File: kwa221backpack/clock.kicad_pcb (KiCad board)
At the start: 2 copper layers, 58.4 x 81.3 mm, 5 parts, among them P1 CONN_01X10, P2 CONN_01X10, U1 TLC5940NT

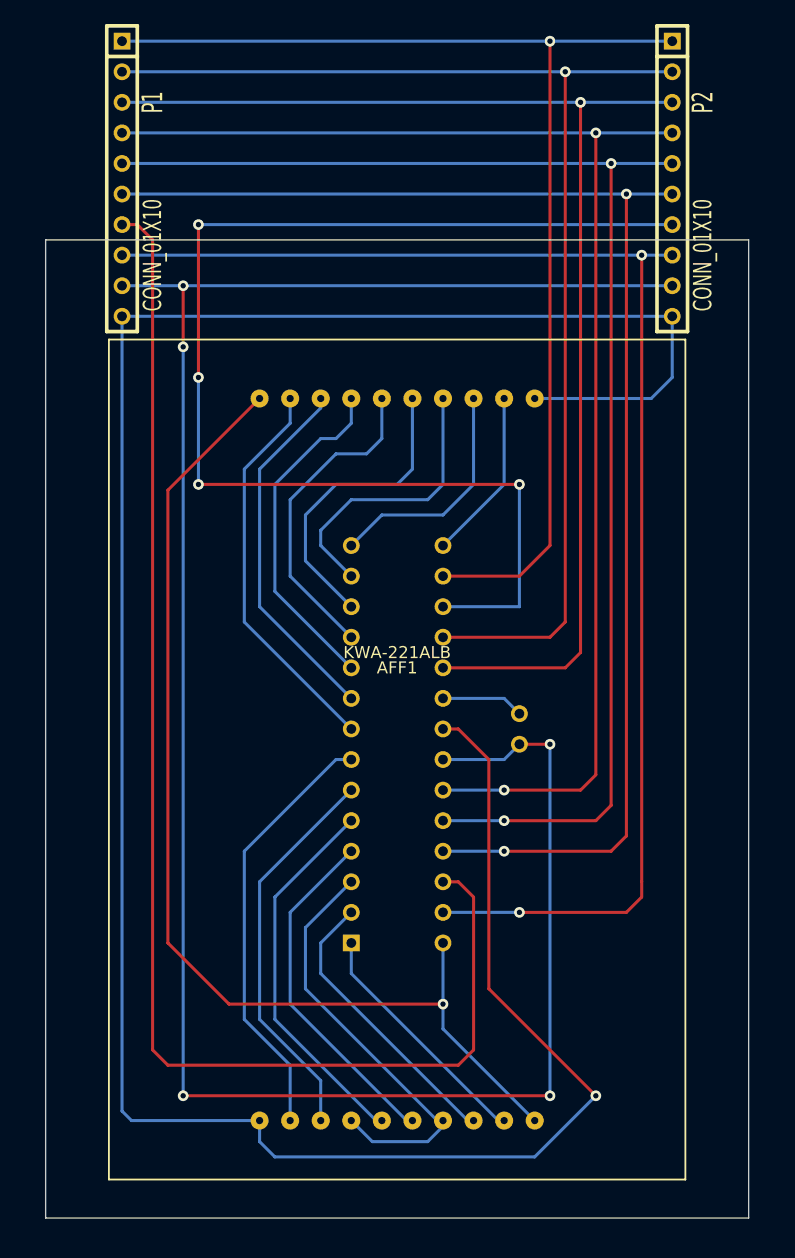
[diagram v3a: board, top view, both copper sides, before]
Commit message: Managed to route all the traces under the LED
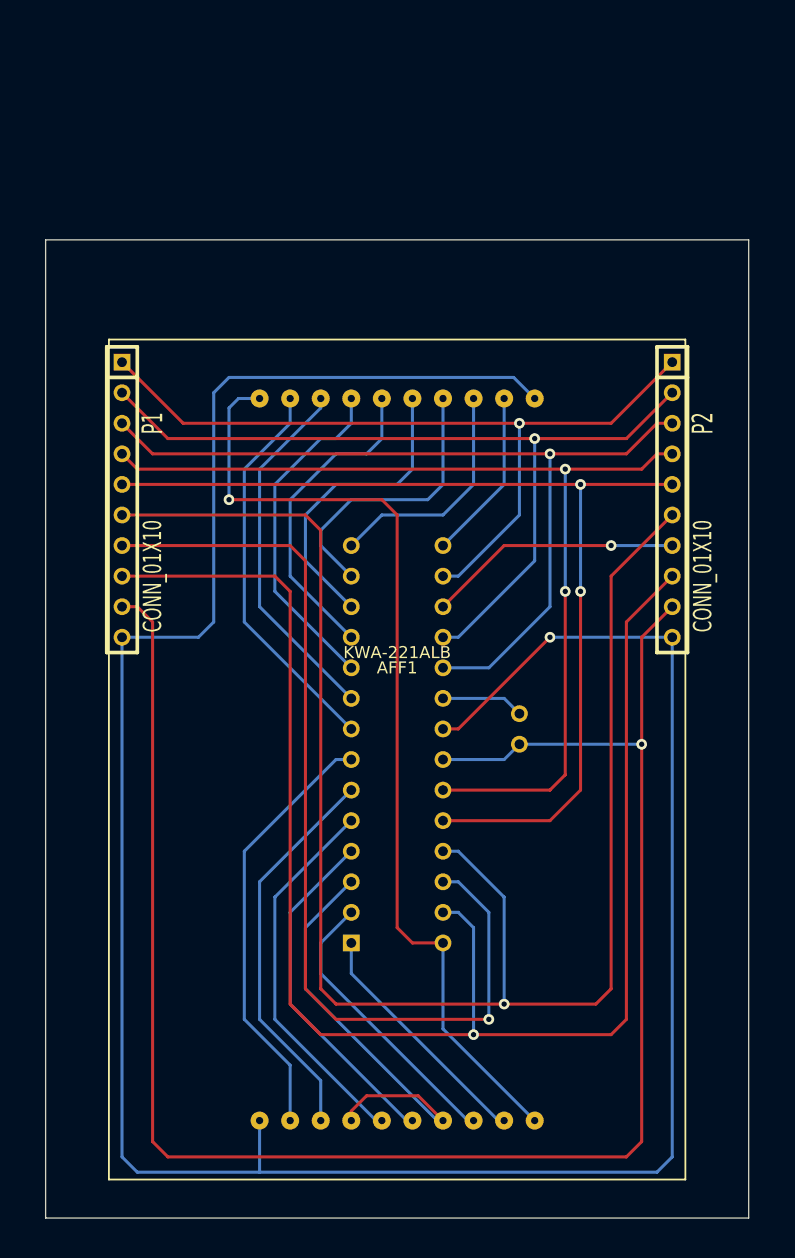
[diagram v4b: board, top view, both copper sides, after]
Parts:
- moved P1 26.7 mm to (49.5, 52.1)
- moved P2 26.7 mm to (95.2, 52.1)
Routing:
- net /SOUT: track 104.1 -> 21.2 mm, vias 4 -> 1
- net /GSCLK: track 102.1 -> 69.3 mm
- net /SIN: track 113.9 -> 81.4 mm, vias 0 -> 1
- net /DCPRG: track 103.4 -> 71.5 mm
- net GND: track 182.1 -> 150.5 mm, vias 5 -> 1
- net /XERR: track 97.6 -> 66.0 mm
- net /XLAT: track 113.6 -> 83.6 mm
- net /BLANK: track 112.3 -> 82.9 mm
- net /SCLK: track 114.8 -> 137.3 mm, vias 2 -> 1
- net /VPRG: track 116.1 -> 128.7 mm, vias 2 -> 1
- net /D0: track 91.3 -> 81.5 mm
- net VCC: track 209.6 -> 214.7 mm

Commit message: More tweaking, allow 3D to render better
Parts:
- P1, P2: moved to B.Cu
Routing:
- net GND: track 150.5 -> 132.7 mm
- net VCC: track 214.7 -> 197.3 mm
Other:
- board size 58.4 x 81.3 mm -> 48.3 x 71.1 mm

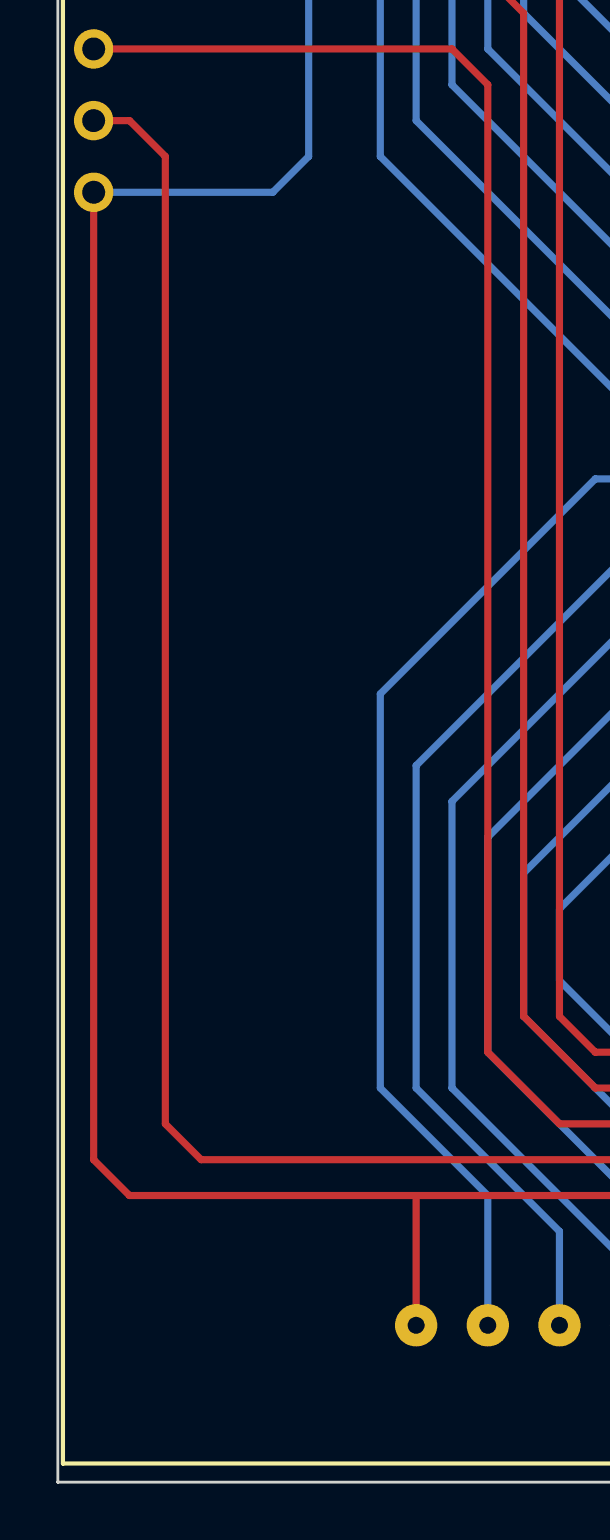
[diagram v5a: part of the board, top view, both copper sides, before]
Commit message: Export Gerber/VRML
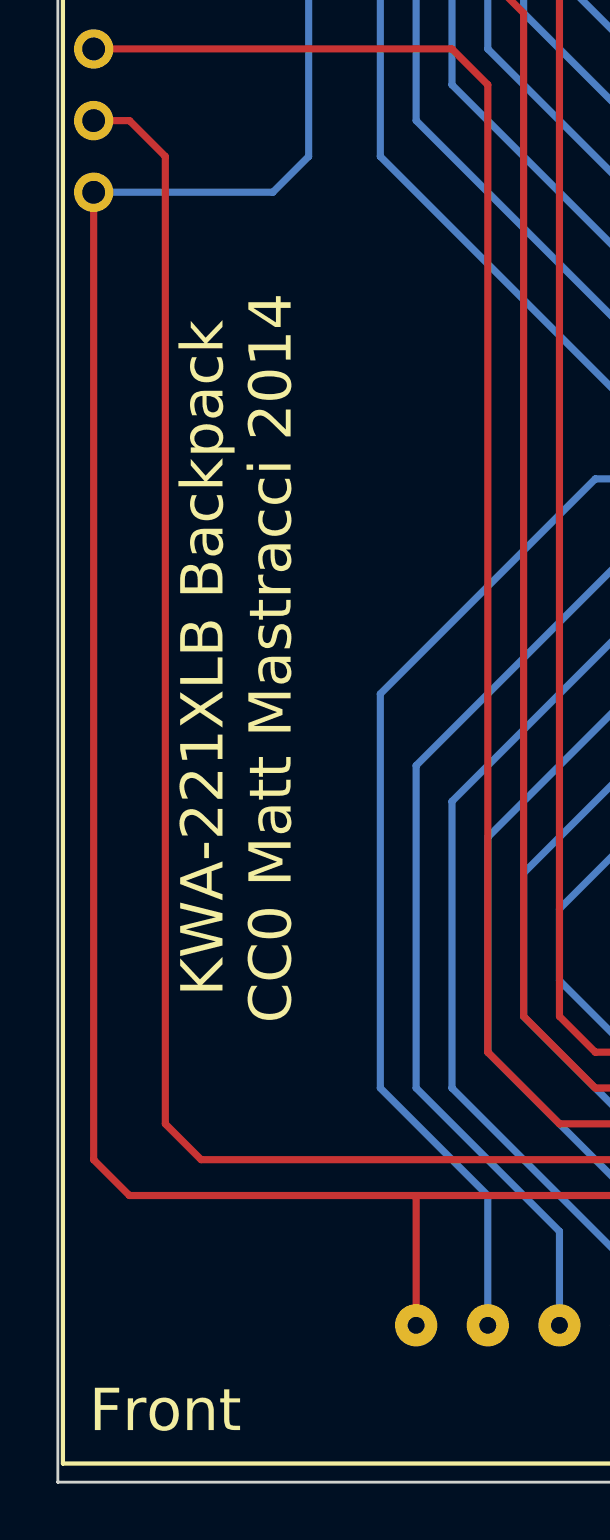
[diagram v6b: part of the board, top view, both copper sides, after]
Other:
- board text added: "Back"
- board text added: "Front"
- board text added: "KWA-221XLB Backpack CC0 Matt Mastracci 2014"
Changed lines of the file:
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@@
     (links 42)
     (no_connects 0)
-    (area 45.71873 38.049999 96.926401 109.270001)
+    (area 39.924287 38.049999 96.926401 109.270001)
     (thickness 1.6)
-    (drawings 4)
+    (drawings 8)
     (tracks 196)
     (zones 0)
@@
       (outputformat 1)
       (mirror false)
-      (drillshape 1)
+      (drillshape 0)
       (scaleselection 1)
-      (outputdirectory ""))
+      (outputdirectory gerber))
   )
   (net 0 "")
@@
     )
   )
+  (gr_text "KWA-221XLB Backpack\nCC0 Matt Mastracci 2014" (at 54.61 80.01 90) (layer B.SilkS)
+    (effects (font (size 1.5 1.5) (thickness 0.3)) (justify mirror))
+  )
+  (gr_text Back (at 92.71 106.68) (layer B.SilkS)
+    (effects (font (size 1.5 1.5) (thickness 0.3)) (justify mirror))
+  )
+  (gr_text Front (at 52.07 106.68) (layer F.SilkS)
+    (effects (font (size 1.5 1.5) (thickness 0.3)))
+  )
+  (gr_text "KWA-221XLB Backpack\nCC0 Matt Mastracci 2014" (at 54.61 80.01 90) (layer F.SilkS)
+    (effects (font (size 1.5 1.5) (thickness 0.3)))
+  )
   (gr_line (start 96.52 38.1) (end 48.26 38.1) (angle 90) (layer Edge.Cuts) (width 0.1))

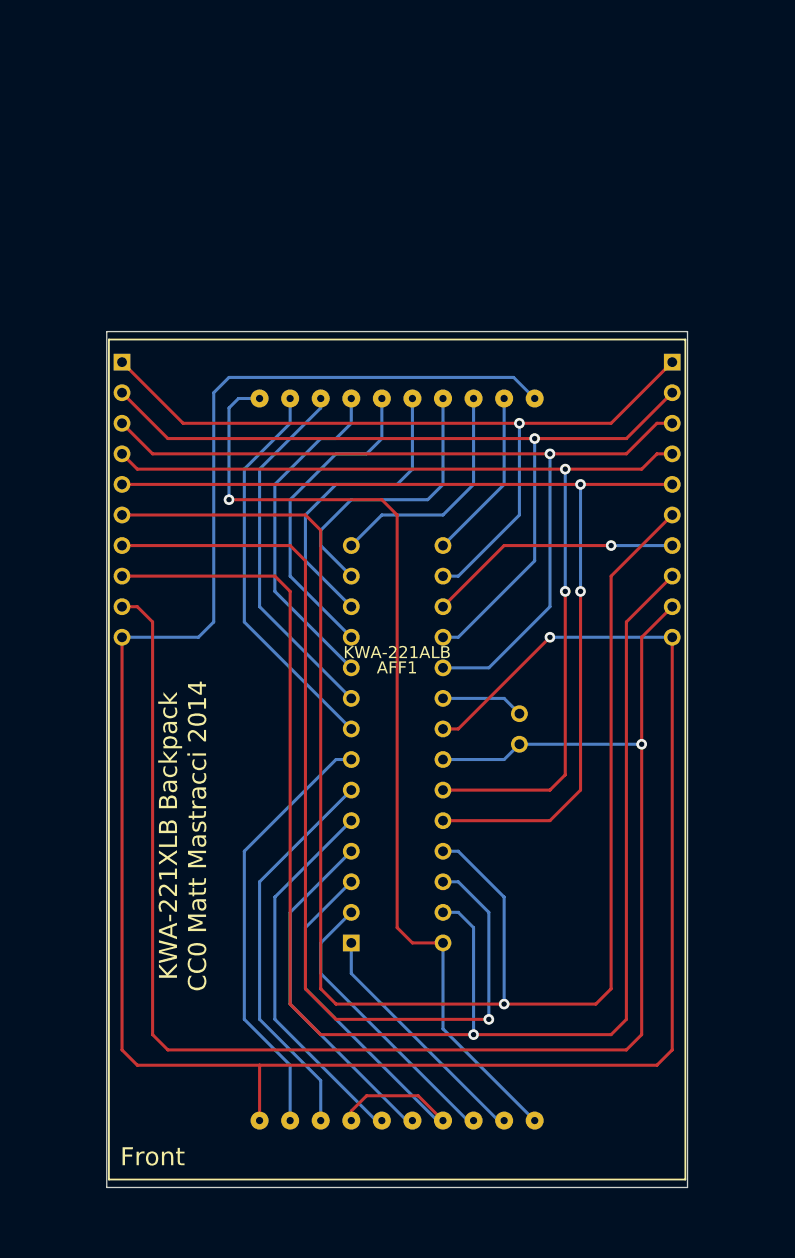
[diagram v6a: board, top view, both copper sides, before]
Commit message: Clean out old VRML/SVG files. Clean up PCB.
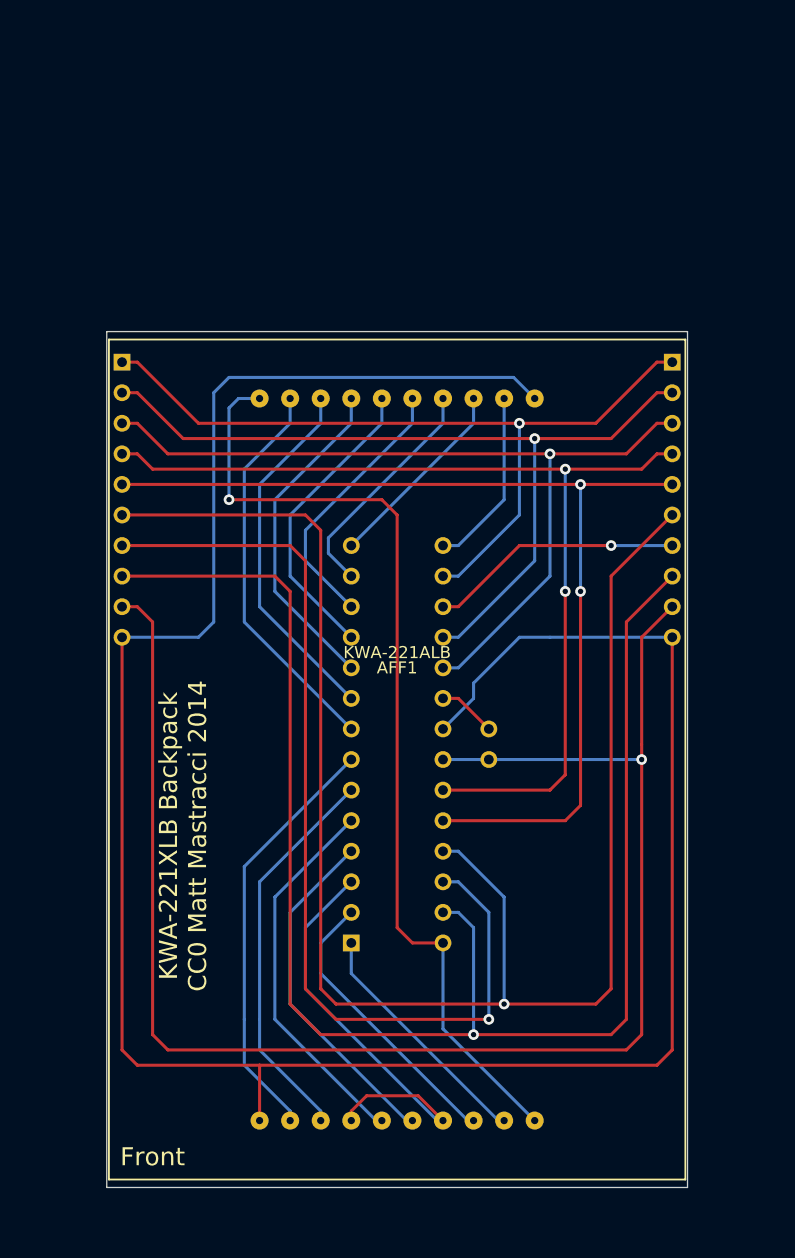
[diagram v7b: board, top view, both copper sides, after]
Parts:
- moved R1 2.84 mm to (80.0, 72.4)
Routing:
- net /D13: track 23.7 -> 19.5 mm
- net /D14: track 19.4 -> 16.4 mm
- net /D12: track 25.5 -> 22.6 mm
- net IREF: track 6.88 -> 4.86 mm
- net /D11: track 26.6 -> 25.1 mm
- net /DCPRG: track 71.5 -> 70.0 mm
- net /D10: track 28.4 -> 27.6 mm
- net /D15: track 14.3 -> 15.1 mm
- net /XLAT: track 83.6 -> 84.3 mm
- net /D7: track 36.0 -> 35.3 mm
- net VCC: track 197.3 -> 198.0 mm, vias 1 -> 0
- net GND: track 132.7 -> 132.2 mm

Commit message: Update schematic for v2: mounting holes and test point to measure iref resistor
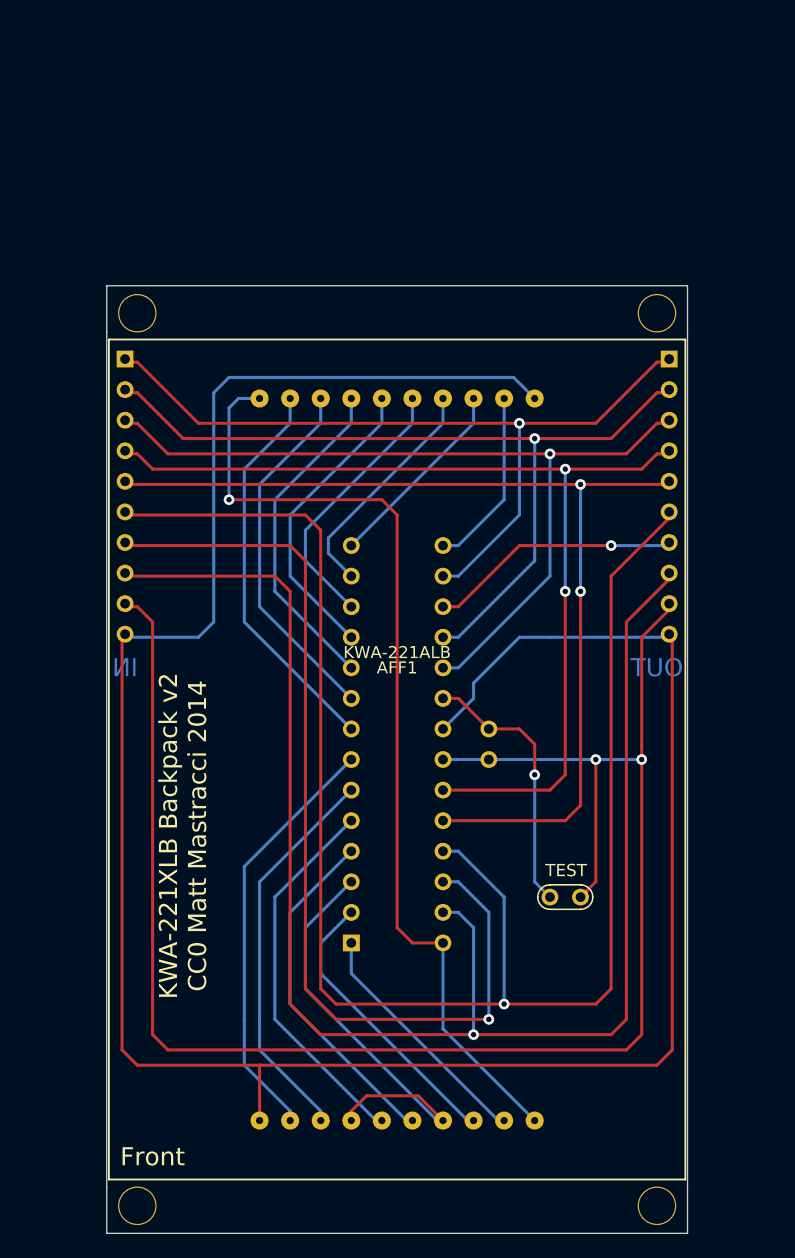
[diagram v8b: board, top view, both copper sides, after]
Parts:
- removed P1, P2: CONN_01X10, SIL-10
- added IN1: , SIL-10, B.Cu at (49.8, 51.8)
- added MH1: MOUNTING_HOLE, 3MM_HOLE, F.Cu at (50.8, 36.6)
- added MH2: MOUNTING_HOLE, 3MM_HOLE, F.Cu at (94.0, 36.6)
- added MH3: MOUNTING_HOLE, 3MM_HOLE, F.Cu at (50.8, 110.7)
- added MH4: MOUNTING_HOLE, 3MM_HOLE, F.Cu at (94.0, 110.7)
- added OUT1: , SIL-10, B.Cu at (95.0, 51.8)
- added W1: TEST, TEST_POINT_2PADS, F.Cu at (86.4, 85.1)
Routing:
- net IREF: track 4.86 -> 22.4 mm, vias 0 -> 1
- net GND: track 132.2 -> 144.1 mm, vias 1 -> 2
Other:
- board size 48.3 x 71.1 mm -> 48.3 x 78.7 mm
- board text added: "BLANK"
- board text added: "DCPRG"
- board text added: "GND"
- board text added: "GSCLK"
- board text added: "IN"
- board text added: "KWA-221XLB Backpack v2 CC0 Matt Mastracci 2014"
- board text added: "OUT"
- board text added: "SCLK"
- board text added: "SIN"
- board text added: "VCC"
- board text added: "VPRG"
- board text added: "XERR"
- board text added: "XLAT"
- board text removed: "KWA-221XLB Backpack CC0 Matt Mastracci 2014"
